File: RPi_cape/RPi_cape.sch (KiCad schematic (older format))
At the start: 109 parts, among them J1 Conn_01x04, J10 Conn_01x02, J11 Conn_01x02, J12 Conn_01x02, J15 Conn_01x06, J16 Conn_01x06, J2 Conn_01x02, J21 Conn_01x06, J3 Conn_01x02, J4 Conn_01x02, J5 Conn_01x03, J6 Conn_01x03, J7 Conn_01x02, J8 Conn_02x20_Odd_Even, J9 Conn_01x02, U1 TL431A, U2 ADC128D818, U3 ADC128D818

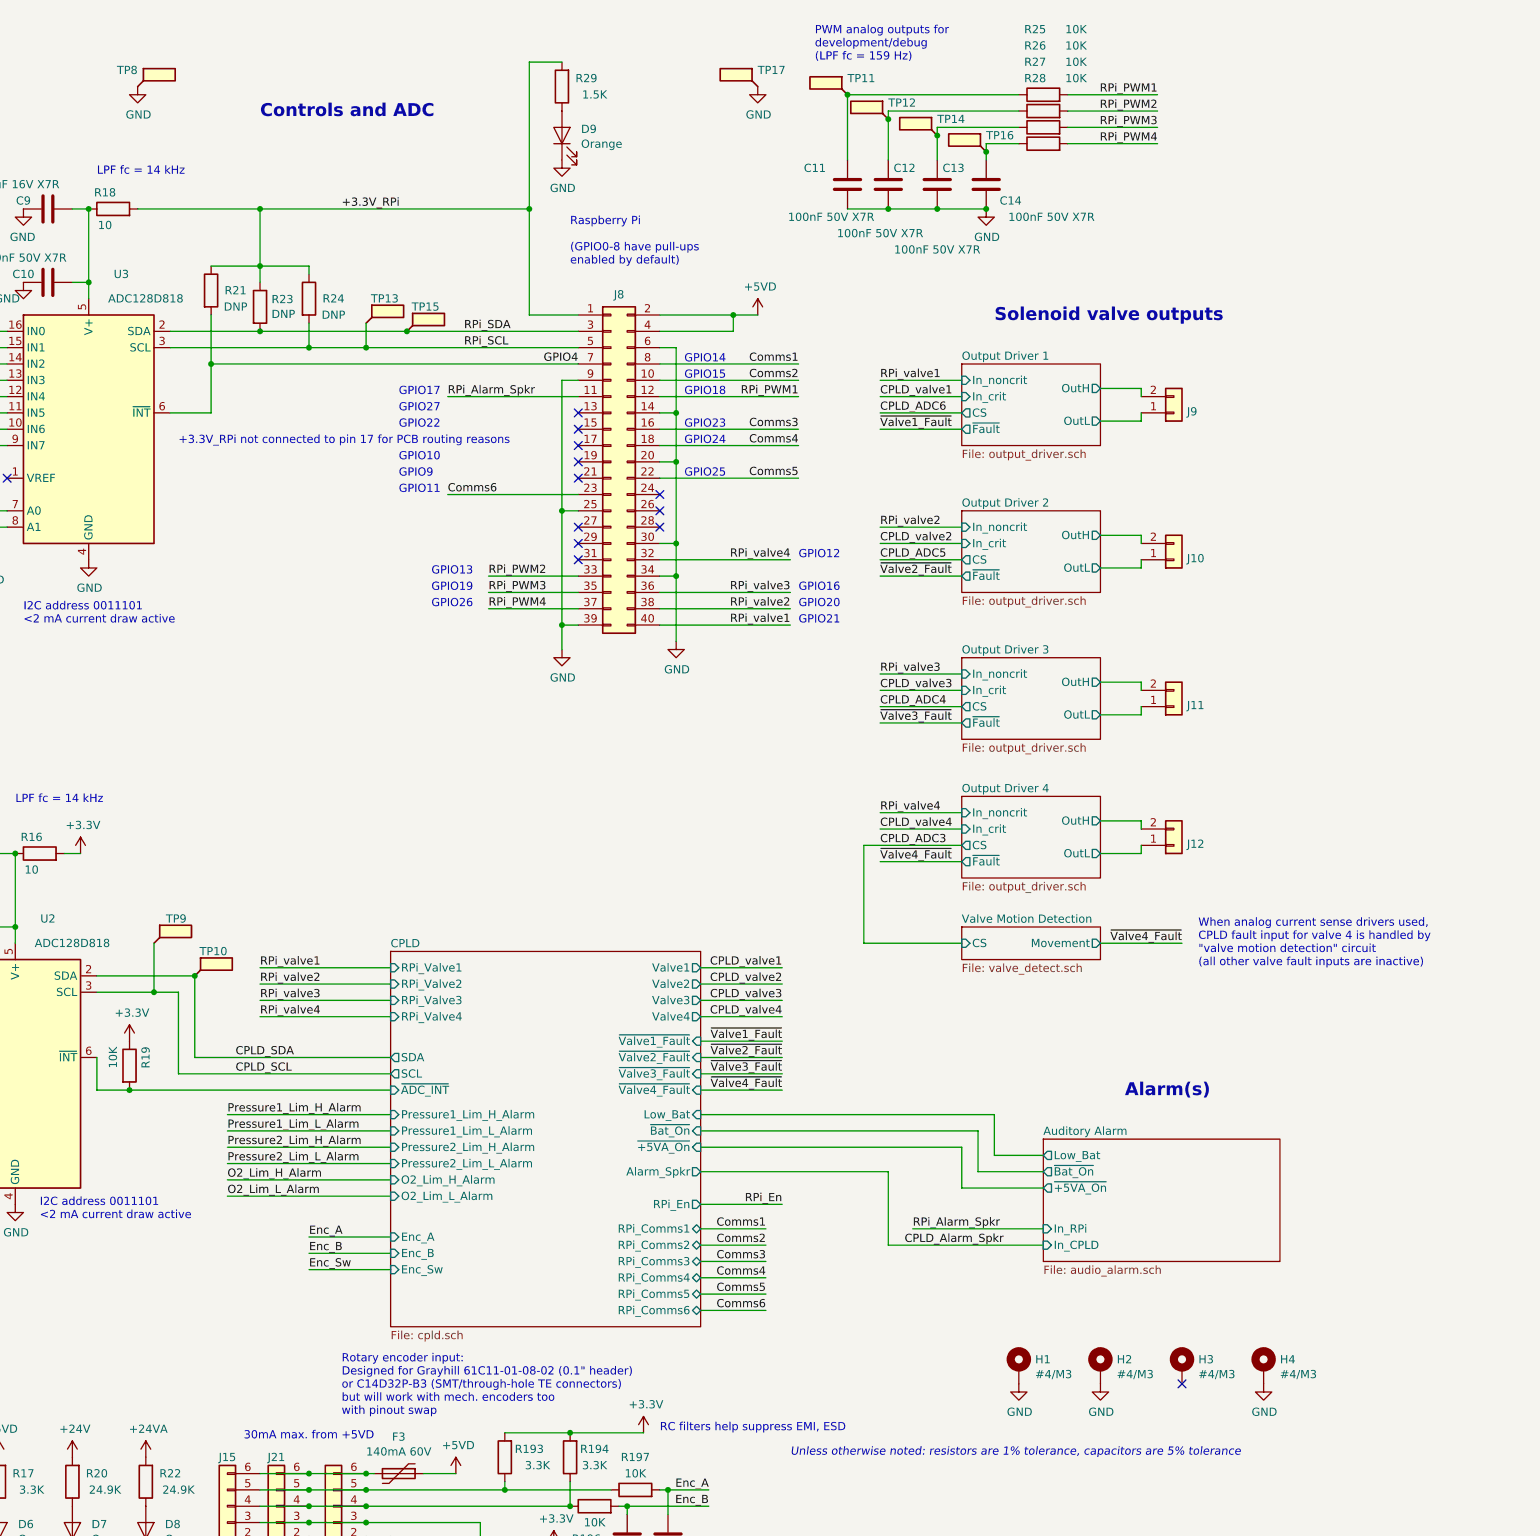
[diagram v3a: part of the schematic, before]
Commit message: Admin (naming, license), improvements based on testing
Updated name on schematic, PCB silkscreen
Added 3 mounting holes on inside area of board for better mechanical robustness
Removed extra unused pressure sensor barb packages from library
Fixed Phoenix spring connector footprints, and added 3D models from Phoenix website
Added 3D models to TE encoder connector footprints, QFP-100 for CPLD, and 5019 testpoint
Changed DIAG_EN pin connection from valve drivers from +24V (too high) to +3.3V
Added CERN licensing terms
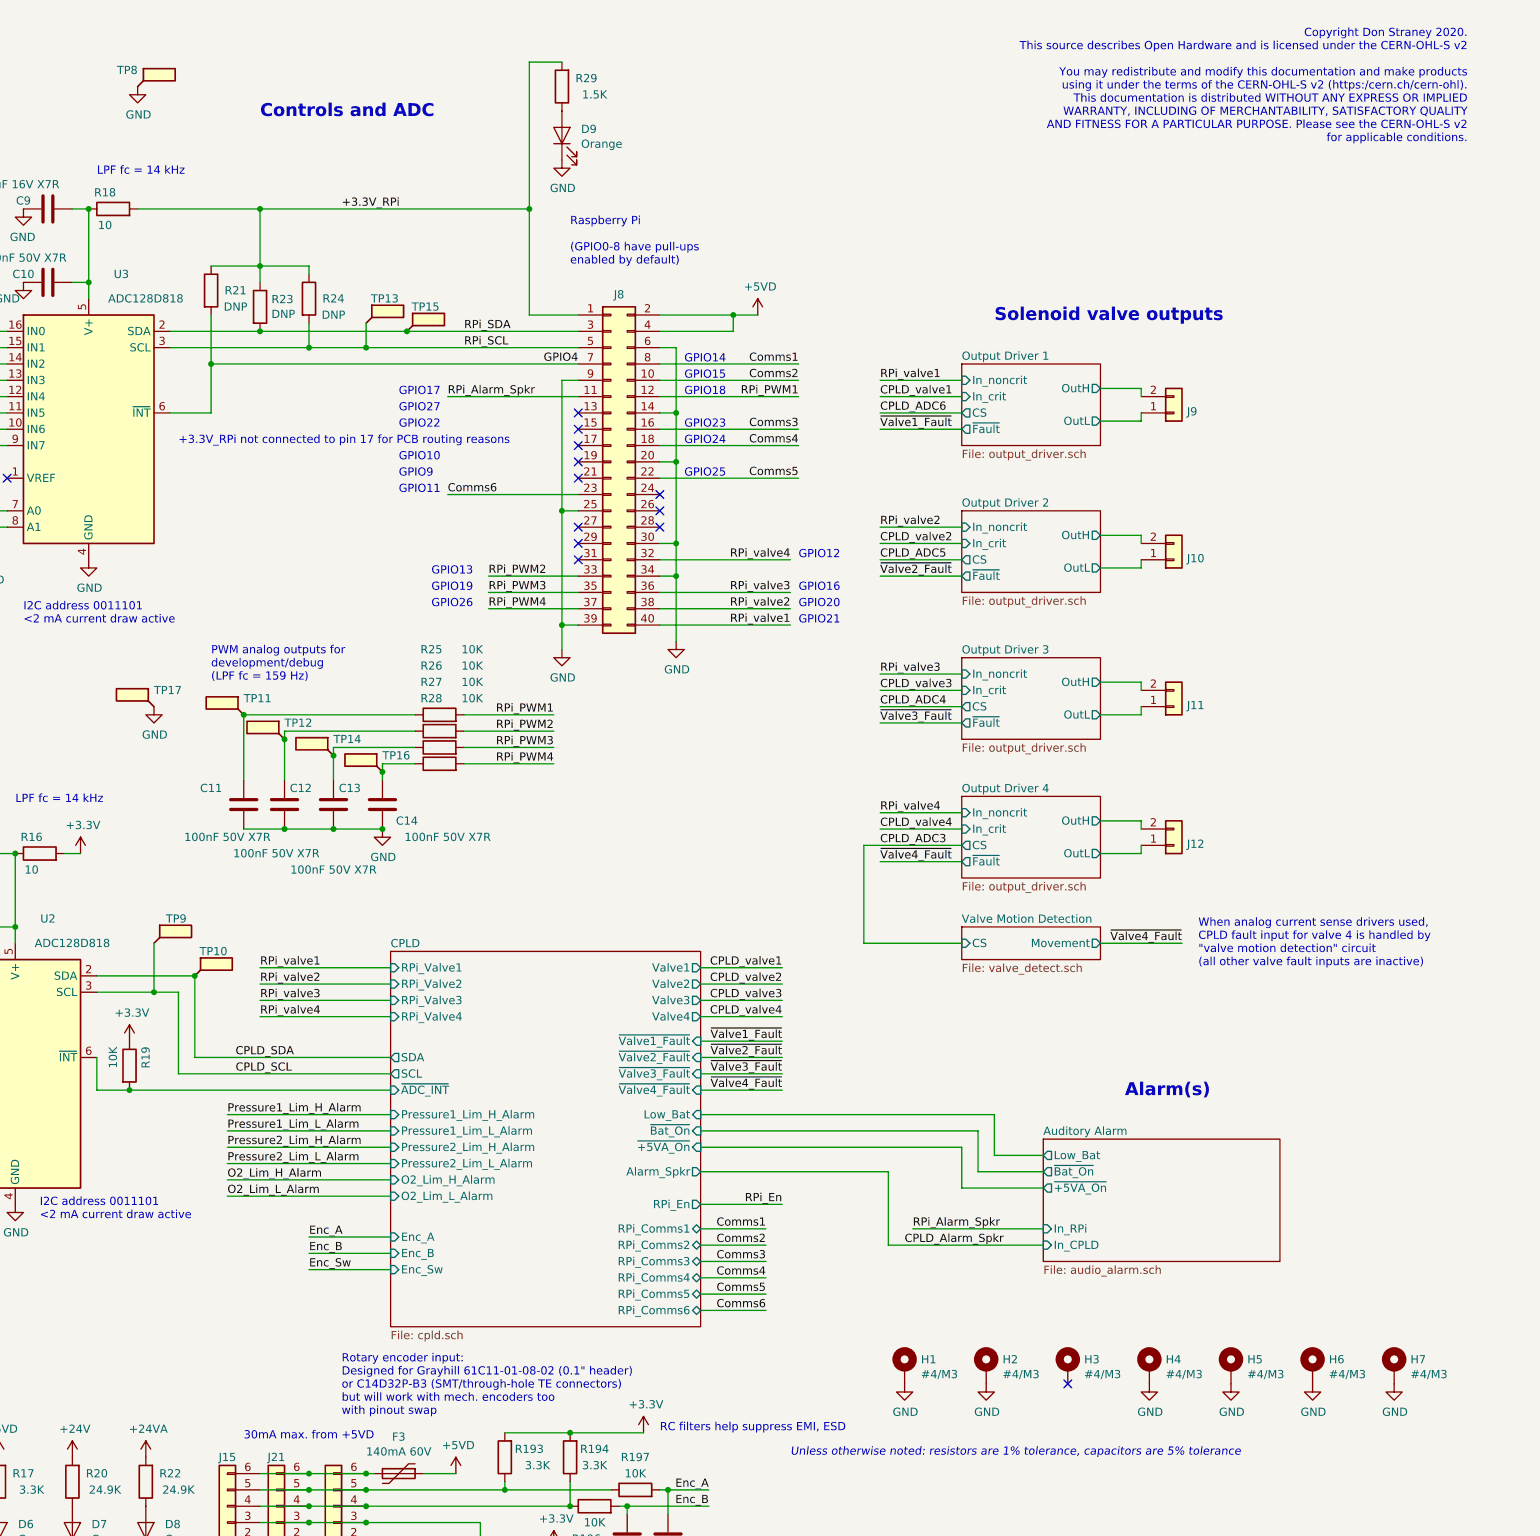
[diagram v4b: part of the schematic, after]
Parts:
- added H5, H6, H7: #4/M3, MountingHole:MountingHole_3.2mm_M3_Pad_Via, symbol Mechanical:MountingHole_Pad
- TP1, TP10, TP11, TP12, TP13, TP14, TP15, TP16, TP17, TP2, TP3, TP4, TP5, TP6, TP7, TP8, TP9: footprint TestPoint:TestPoint_Keystone_5019_Minature -> Ventilator:TestPoint_Keystone_5019_Minature
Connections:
- net GND: now also H5.1, H6.1, H7.1
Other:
- note added: "Copyright Don Straney 2020.\nThis source describes Open Hardware and is licensed under the CERN-OHL-S v2\n\nYou may redistribute and modify this documentation and make products\nusing it under the terms of the CERN-OHL-S v2 (https:/cern.ch/cern-ohl).\nThis documentation is distributed WITHOUT ANY EXPRESS OR IMPLIED\nWARRANTY, INCLUDING OF MERCHANTABILITY, SATISFACTORY QUALITY\nAND FITNESS FOR A P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"
- moved on the sheet: C11, C12, C13, C14, H1, H2, H3, H4, R25, R26, R27, R28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

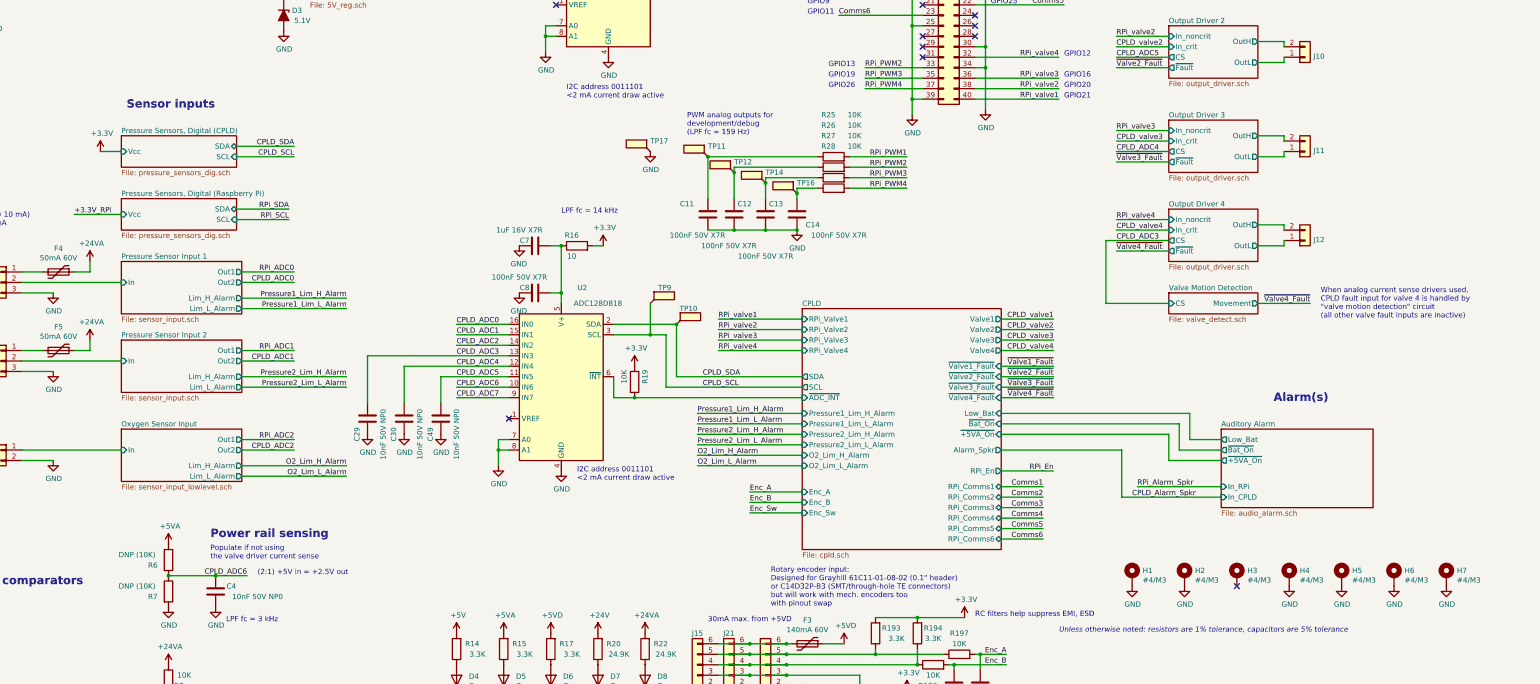
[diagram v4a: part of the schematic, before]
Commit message: Design update based on changed software/firmware/pneumatics reqs
Swapped Max V CPLD for Max 10 FPGA
Removed +1.8V regulator and monitoring (in power-down alarm) because Max 10 FPGA has internal regulator
Changed FPGA's valve-enable pull-downs from 1K to 10K because Max 10 floats the outputs during power-up/programming (instead of Max V's internal pull-ups)
Changed low-pressure sensor from BMP388 to MS5607 for more manufacturable footprint / high availability, and moved all digital pressure sensors to daughterboard for repairability
Changed single op-amps in analog pressure sensor inputs / valve motion detect circuits to TLV6001 for better bias current, correct footprint
Removed excessive DNP components in analog pressure sensor inputs to ease routing with new op-amps
Added double-inverted hysteresis circuit to valve motion detect that won't drive U38's '+' input above the rail and cause latchup
Added optional pull-down resistors to valve-motiion-detect op-amps to allow output voltages to swing to zero
Added optional filter caps to ADC sensor inputs
Added pull-down to O2 sensor input for testing with sensor unplugged
Increased ADC input resistors (in analog sensor inputs) from 1K to 3.3K to avoid "lifting" +3.3V rail voltage in case of fault
Increased hole sizes to 3.7 mm for fitting #6 screws, to match some threaded vibration-damping bumpers from Joost
Fixed F.Fab-layer component reference text in custom footprints
Updated manufacturing files
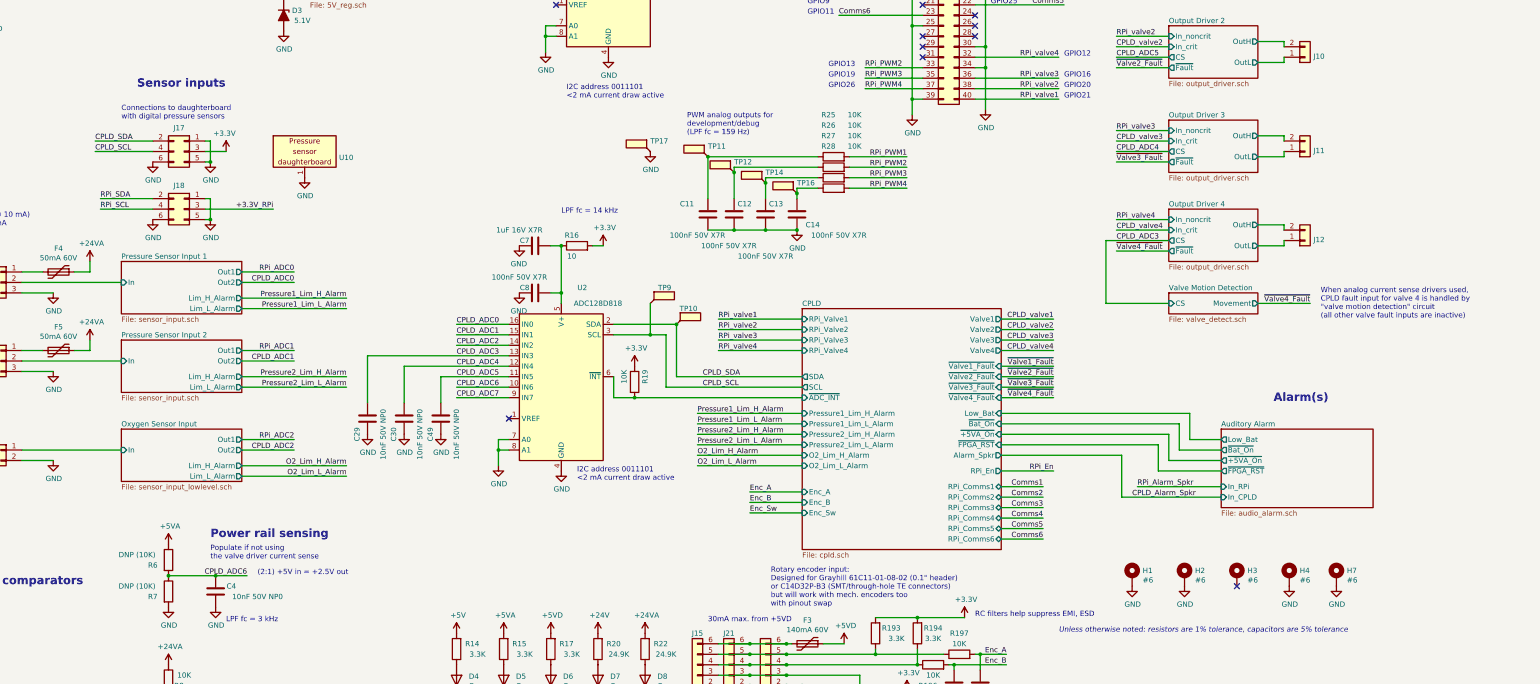
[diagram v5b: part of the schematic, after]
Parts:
- removed H5, H6: #4/M3, MountingHole:MountingHole_3.2mm_M3_Pad_Via, symbol Mechanical:MountingHole_Pad
- added J17, J18: Conn_02x03_Odd_Even, Connector_PinHeader_2.54mm:PinHeader_2x03_P2.54mm_Vertical_SMD, symbol Connector_Generic:Conn_02x03_Odd_Even
- added U10: Pressure_sensor_daughterboard, Ventilator:Pressure_sensor_daughterboard_1.2, symbol Ventilator:Pressure_sensor_daughterboard
- C1, D23, F1, J1, J10, J11, J12, J15, J16, J2, J21, J3, J4, J5, J6, J7, J8, J9, R21, R23, R24, R3, R6, R7: DNI (none) -> DNI
- H1, H2, H3, H4, H7: value #4/M3 -> #6; footprint MountingHole:MountingHole_3.2mm_M3_Pad_Via -> MountingHole:MountingHole_3.7mm_Pad_Via
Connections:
- net +3.3V_RPi: now also J18.3 (Pin_3)
- net +3V3: now also J17.3 (Pin_3)
- net CPLD_SCL: now also J17.4 (Pin_4)
- net CPLD_SDA: now also J17.2 (Pin_2)
- net GND: now also J17.1 (Pin_1), J17.5 (Pin_5), J17.6 (Pin_6), J18.1 (Pin_1), J18.5 (Pin_5), J18.6 (Pin_6), U10.1
- net RPi_SCL: now also J18.4 (Pin_4)
- net RPi_SDA: now also J18.2 (Pin_2)
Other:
- note added: "Connections to daughterboard\nwith digital pressure sensors"
- moved on the sheet: H7
